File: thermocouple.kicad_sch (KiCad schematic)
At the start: 14 parts, among them U1 AD8495

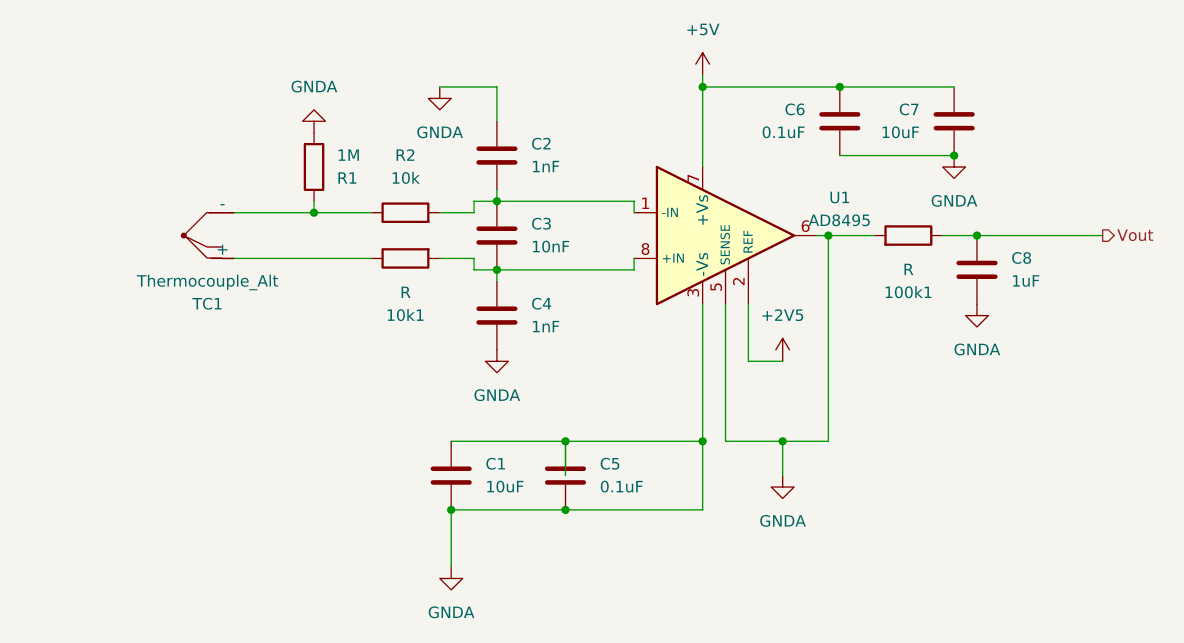
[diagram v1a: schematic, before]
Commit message: added footprints to almost all components
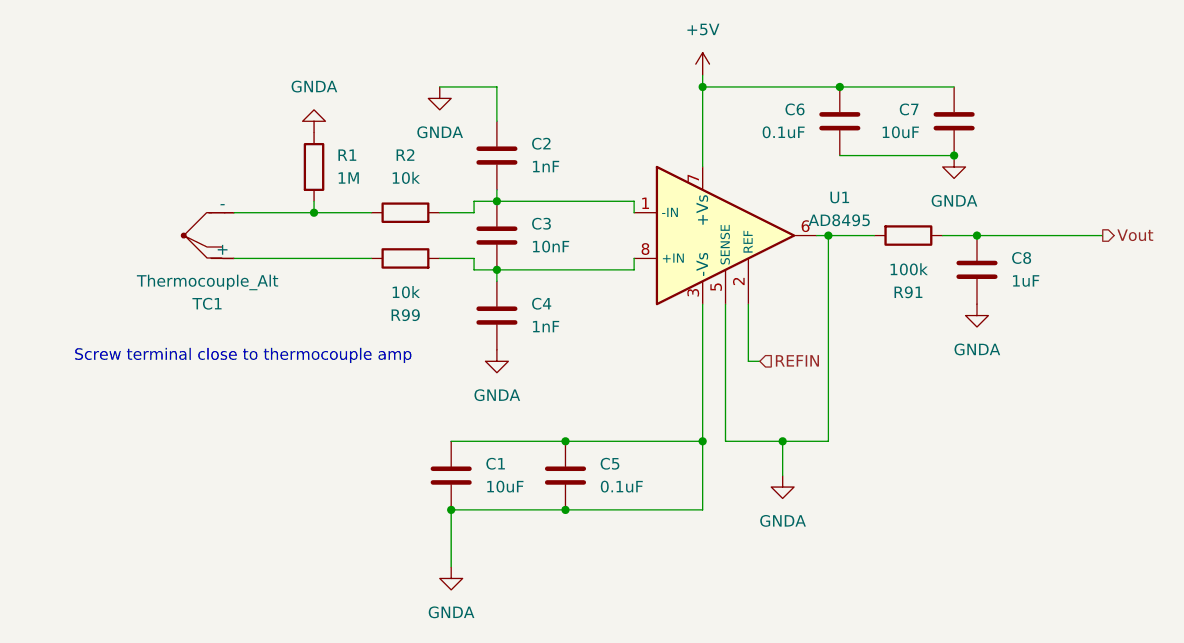
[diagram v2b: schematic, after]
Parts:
- removed 100k1, 10k1: R, symbol Device:R
- added R91: 100k, Resistor_SMD:R_0805_2012Metric_Pad1.20x1.40mm_HandSolder, symbol Device:R
- added R99: 10k, Resistor_SMD:R_0805_2012Metric_Pad1.20x1.40mm_HandSolder, symbol Device:R
- C1, C2, C3, C4, C5, C6, C7, C8: footprint (none) -> Capacitor_SMD:C_0603_1608Metric_Pad1.08x0.95mm_HandSolder
- R1, R2: footprint (none) -> Resistor_SMD:R_0805_2012Metric_Pad1.20x1.40mm_HandSolder
- TC1: footprint (none) -> Connector_JST:JST_GH_BM02B-GHS-TBT_1x02-1MP_P1.25mm_Vertical
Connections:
- net GNDA: now also R1.1, R91.2; no longer R1.2
- net Vout: now also R91.1
- net at C3.2, C4.1, U1.8 (+IN): now also R99.2
- net at TC1.1 (+): now also R99.1
- net at R2.1, TC1.2 (-): now also R1.2; no longer R1.1
- net +2V5 renamed REFIN
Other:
- note added: "Screw terminal close to thermocouple amp"
